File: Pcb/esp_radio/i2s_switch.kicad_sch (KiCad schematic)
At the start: 10 parts, among them U7 74HC157, U8 74HC157

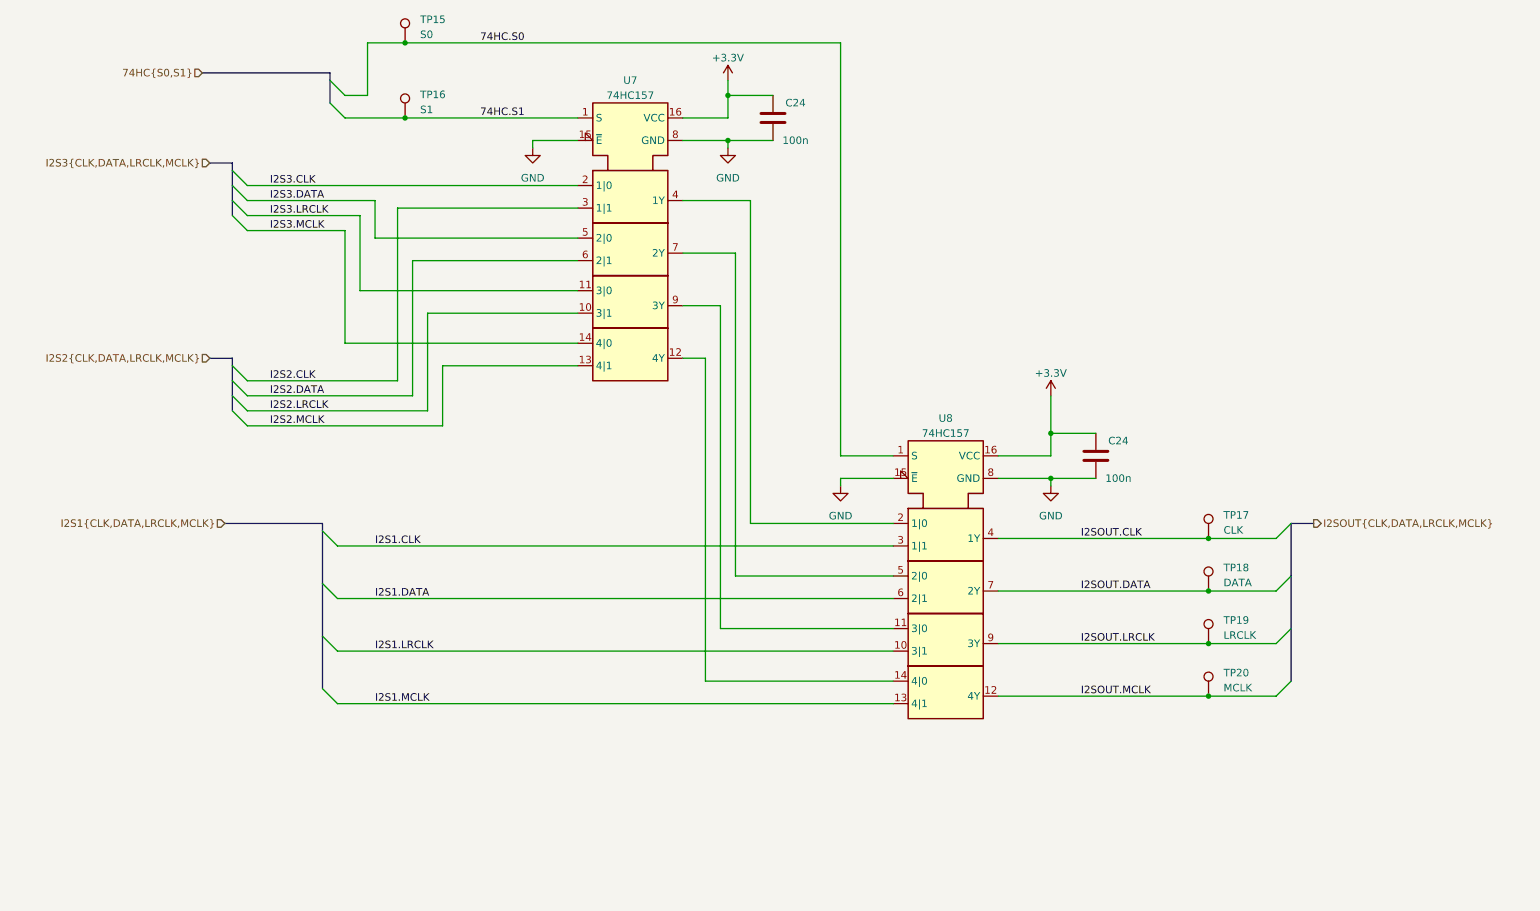
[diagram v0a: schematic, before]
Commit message: Move custom components to kicad_common_library.
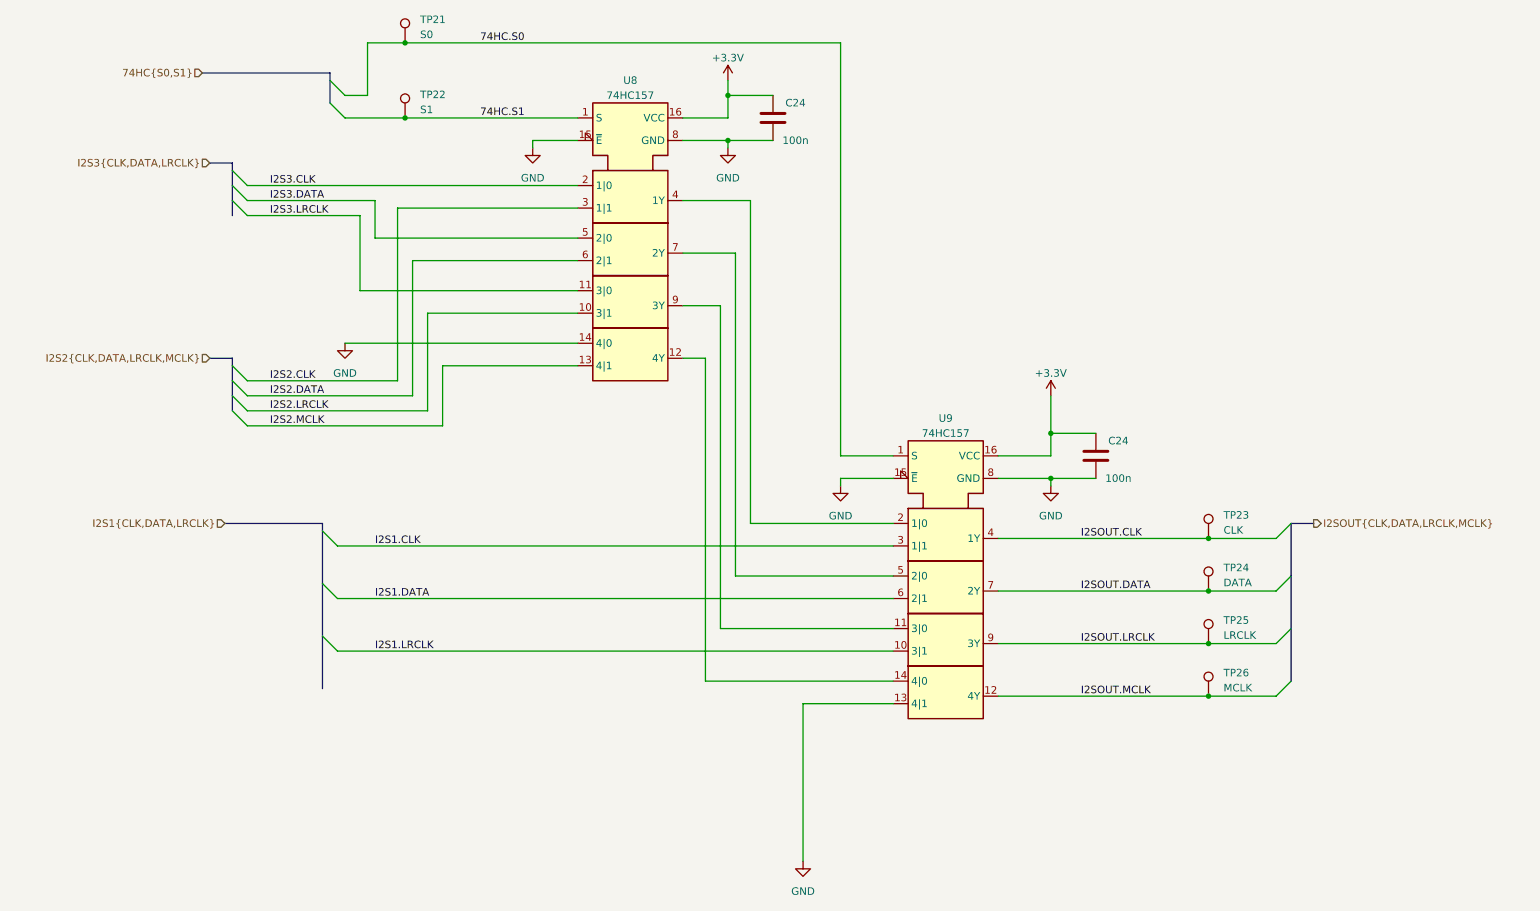
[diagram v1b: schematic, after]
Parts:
- U8: renamed from U7; symbol 74hc157:74HC157 -> kicad_common_lib:74HC157
- U9: renamed from U8; symbol 74hc157:74HC157 -> kicad_common_lib:74HC157
- renumbered TP15 to TP21, TP16 to TP22, TP17 to TP23, TP18 to TP24, TP19 to TP25, TP20 to TP26
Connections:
- net I2S1.MCLK is gone; now on net GND: U9.13 (4|1)
- net I2S3.MCLK is gone; now on net GND: U8.14 (4|0)

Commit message: Add components layout on PCB
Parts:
- C24: footprint (none) -> kicad_common_lib:C_0805
- TP21, TP22, TP23, TP24, TP25, TP26: footprint (none) -> TestPoint:TestPoint_THTPad_D2.0mm_Drill1.0mm
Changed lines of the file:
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@@
       (effects (font (size 1.27 1.27)) (justify left))
     )
-    (property "Footprint" "" (at 234.95 142.24 0)
+    (property "Footprint" "TestPoint:TestPoint_THTPad_D2.0mm_Drill1.0mm" (at 234.95 142.24 0)
       (effects (font (size 1.27 1.27)) hide)
     )
@@
       (effects (font (size 1.27 1.27)))
     )
-    (property "Footprint" "" (at 157.1752 48.26 0)
+    (property "Footprint" "kicad_common_lib:C_0805" (at 157.1752 48.26 0)
       (effects (font (size 1.27 1.27)) hide)
     )
@@
       (effects (font (size 1.27 1.27)) (justify left))
     )
-    (property "Footprint" "" (at 234.95 124.46 0)
+    (property "Footprint" "TestPoint:TestPoint_THTPad_D2.0mm_Drill1.0mm" (at 234.95 124.46 0)
       (effects (font (size 1.27 1.27)) hide)
     )
@@
       (effects (font (size 1.27 1.27)) (justify left))
     )
-    (property "Footprint" "" (at 234.95 115.57 0)
+    (property "Footprint" "TestPoint:TestPoint_THTPad_D2.0mm_Drill1.0mm" (at 234.95 115.57 0)
       (effects (font (size 1.27 1.27)) hide)
     )
@@
       (effects (font (size 1.27 1.27)))
     )
-    (property "Footprint" "" (at 211.7852 105.41 0)
+    (property "Footprint" "kicad_common_lib:C_0805" (at 211.7852 105.41 0)
       (effects (font (size 1.27 1.27)) hide)
     )
@@
       (effects (font (size 1.27 1.27)) (justify left))
     )
-    (property "Footprint" "" (at 99.06 31.75 0)
+    (property "Footprint" "TestPoint:TestPoint_THTPad_D2.0mm_Drill1.0mm" (at 99.06 31.75 0)
       (effects (font (size 1.27 1.27)) hide)
     )
@@
       (effects (font (size 1.27 1.27)) (justify left))
     )
-    (property "Footprint" "" (at 234.95 133.35 0)
+    (property "Footprint" "TestPoint:TestPoint_THTPad_D2.0mm_Drill1.0mm" (at 234.95 133.35 0)
       (effects (font (size 1.27 1.27)) hide)
     )
@@
       (effects (font (size 1.27 1.27)) (justify left))
     )
-    (property "Footprint" "" (at 99.06 44.45 0)
-      (effects (font (size 1.27 1.27)) hide)
-    )
+    (property "Footprint" "TestPoint:TestPoint_THTPad_D2.0mm_Drill1.0mm" (at 99.06 44.45 0)
+      (effects (font (size 1.27 1.27)) hide)
+    )
